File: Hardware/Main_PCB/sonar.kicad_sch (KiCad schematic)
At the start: 11 parts, among them U2 TUSS4470TRTJT

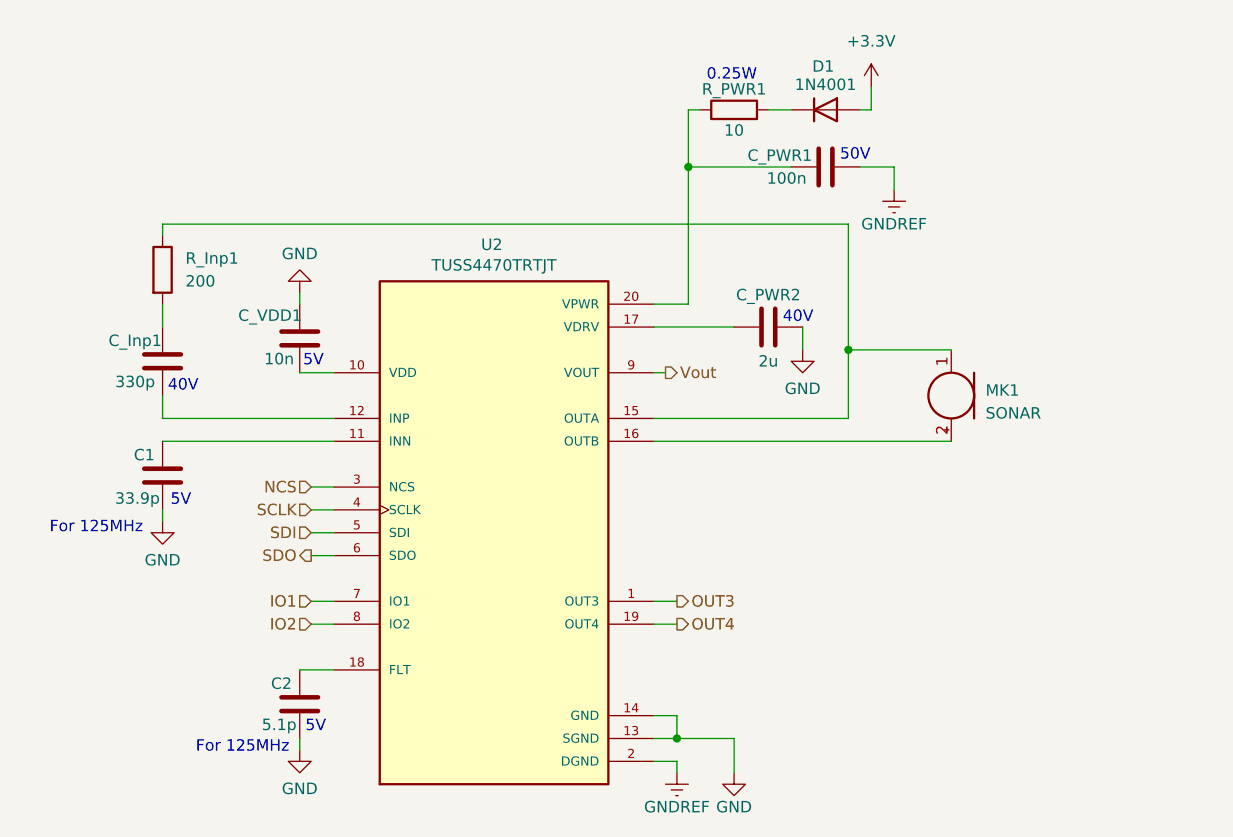
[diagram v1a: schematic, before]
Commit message: Trustworthy version of the MAIN PCB schematic
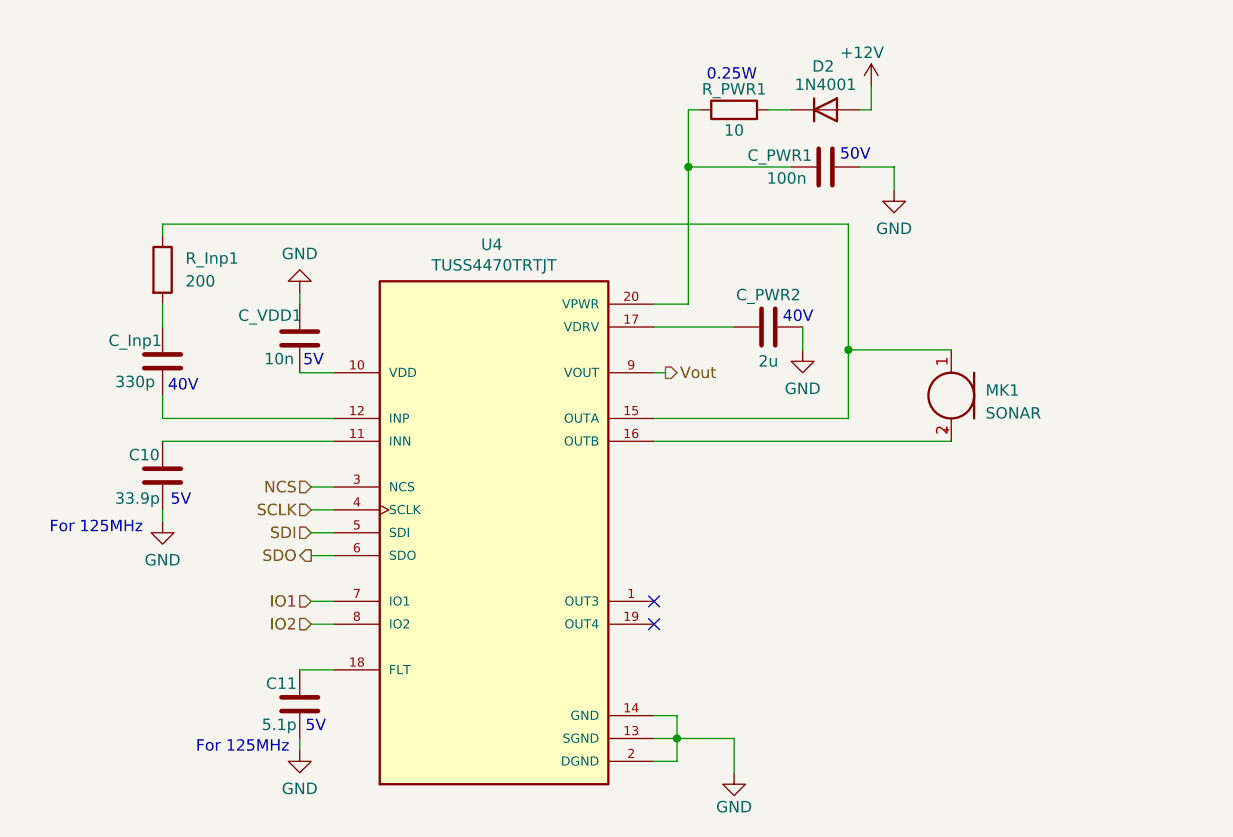
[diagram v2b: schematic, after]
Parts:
- renumbered C1 to C10, C2 to C11, D1 to D2, U2 to U4
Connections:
- net GNDREF is gone; now on net GND: C_PWR1.2, U4.2 (DGND)
- net +3.3V renamed +12V
- net OUT3: no longer names the net of U4.1 (OUT3)
- net OUT4: no longer names the net of U4.19 (OUT4)
- no-connect marks 0 -> 2

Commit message: Added some footprints
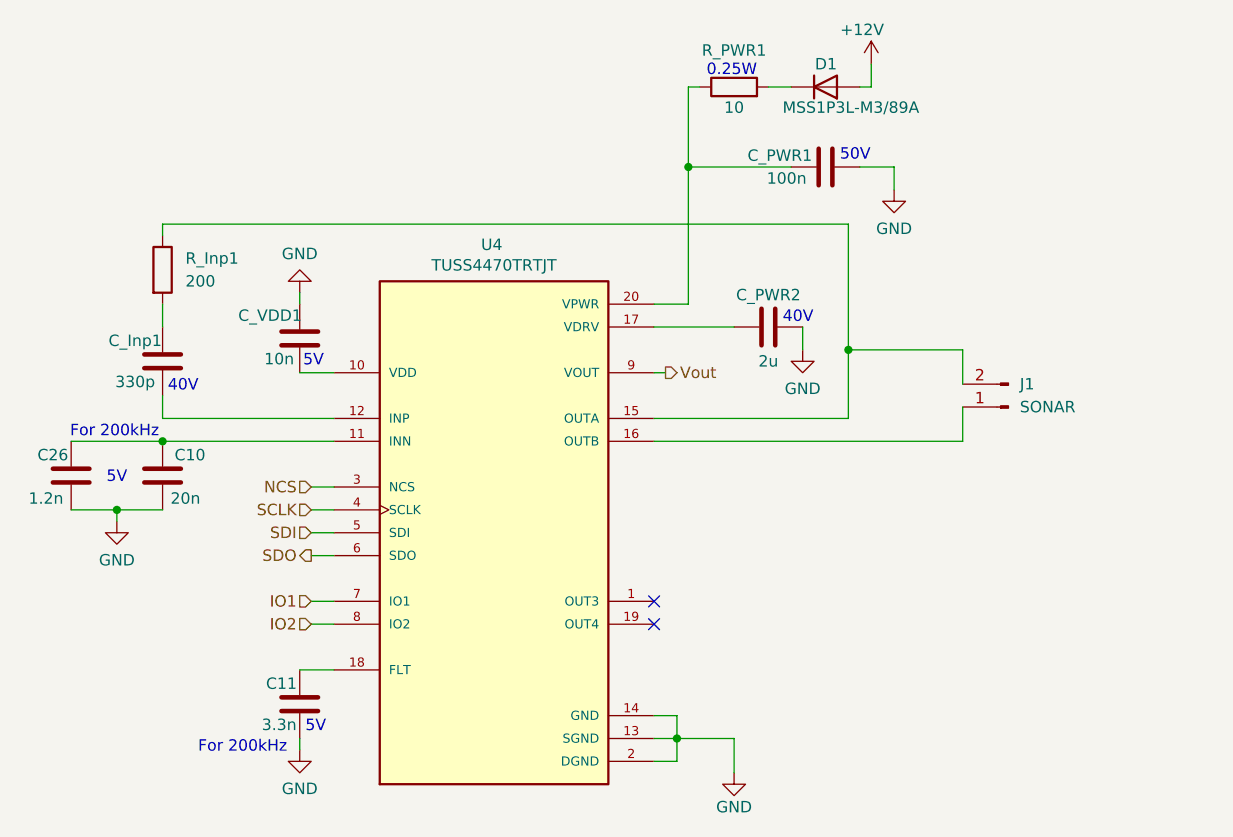
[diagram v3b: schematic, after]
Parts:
- removed D2: 1N4001, symbol Device:D
- removed MK1: SONAR, symbol Device:Microphone
- added C26: 1.2n, Capacitor_SMD:C_0603_1608Metric_Pad1.08x0.95mm_HandSolder, symbol Device:C
- added D1: MSS1P3L-M3/89A, Diode_SMD:Vishay_SMPA, symbol Diode:S2JTR
- added J1: SONAR, Connector_JST:JST_PH_B2B-PH-K_1x02_P2.00mm_Vertical, symbol Connector:Conn_01x02_Pin
- C10: value 33.9p -> 20n; footprint (none) -> Capacitor_SMD:C_0805_2012Metric_Pad1.18x1.45mm_HandSolder
- C11: value 5.1p -> 3.3n; footprint (none) -> Capacitor_SMD:C_0805_2012Metric_Pad1.18x1.45mm_HandSolder
- C_Inp1, C_PWR1, C_VDD1, R_PWR1: footprint (none) -> Capacitor_SMD:C_0805_2012Metric_Pad1.18x1.45mm_HandSolder
- C_PWR2: footprint (none) -> Capacitor_SMD:C_0603_1608Metric_Pad1.08x0.95mm_HandSolder
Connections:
- net +12V: now also D1.2 (A)
- net GND: now also C26.1
- net at C10.2, U4.11 (INN): now also C26.2
- net at R_Inp1.1, U4.15 (OUTA): now also J1.2 (Pin_2)
- net at U4.16 (OUTB): now also J1.1 (Pin_1)
- net at R_PWR1.2: now also D1.1 (K)
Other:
- note added: "For 200kHz"
- note removed: "For 125MHz"
- moved on the sheet: R_PWR1

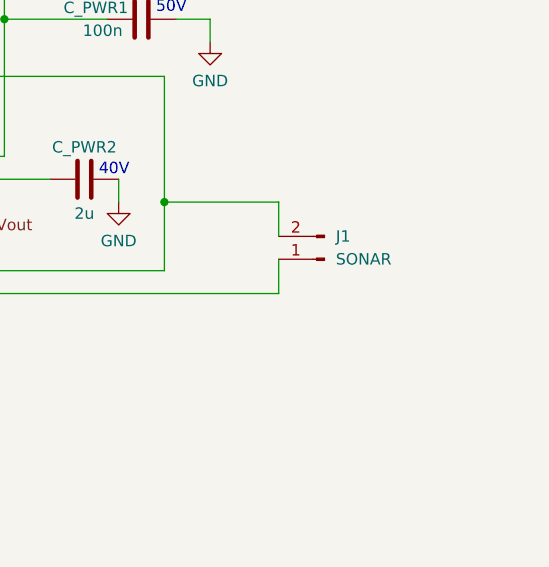
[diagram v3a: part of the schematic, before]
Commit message: Updated sonar.kicad_sch with a new sonar connector
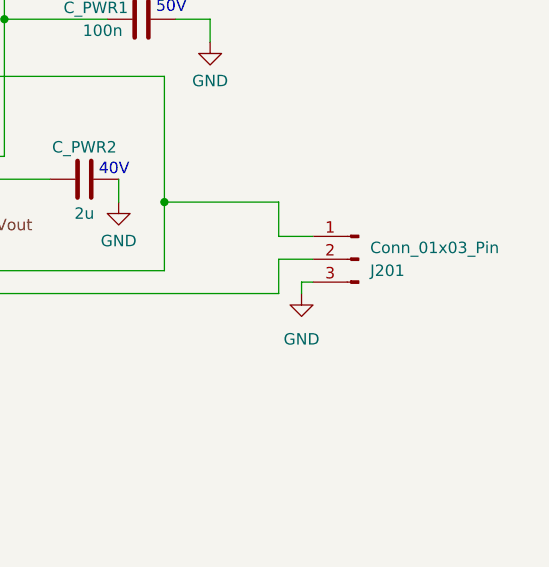
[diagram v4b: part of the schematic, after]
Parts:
- removed J1: SONAR, Connector_JST:JST_PH_B2B-PH-K_1x02_P2.00mm_Vertical, symbol Connector:Conn_01x02_Pin
- added J201: Conn_01x03_Pin, Connector_JST:JST_PH_B3B-PH-K_1x03_P2.00mm_Vertical, symbol Connector:Conn_01x03_Pin
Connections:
- net GND: now also J201.3 (Pin_3)
- net at R_Inp1.1, U4.15 (OUTA): now also J201.1 (Pin_1)
- net at U4.16 (OUTB): now also J201.2 (Pin_2)
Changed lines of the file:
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@@
+	(wire
+		(pts
+			(xy 143.51 57.15) (xy 147.32 57.15)
+		)
+		(stroke
+			(width 0)
+			(type default)
+		)
+	)
 	(wire
 		(pts
@@
 	(wire
 		(pts
+			(xy 146.05 59.69) (xy 146.05 60.96)
+		)
+		(stroke
+			(width 0)
+			(type default)
+		)
+	)
+	(wire
+		(pts
 			(xy 143.51 50.8) (xy 143.51 54.61)
 		)
@@
 	(wire
 		(pts
+			(xy 146.05 59.69) (xy 147.32 59.69)
+		)
+		(stroke
+			(width 0)
+			(type default)
+		)
+	)
+	(wire
+		(pts
 			(xy 113.03 30.48) (xy 124.46 30.48)
 		)
@@
 		(pts
 			(xy 109.22 53.34) (xy 110.49 53.34)
+		)
+		(stroke
+			(width 0)
+			(type default)
+		)
+	)
+	(wire
+		(pts
+			(xy 143.51 54.61) (xy 147.32 54.61)
 		)
 		(stroke
@@
 	)
 	(symbol
+		(lib_id "Connector:Conn_01x03_Pin")
+		(at 152.4 57.15 0)
+		(mirror y)
+		(unit 1)
+		(exclude_from_sim no)
+		(in_bom yes)
+		(on_board yes)
+		(dnp no)
+		(property "Reference" "J201"
+			(at 153.67 58.4201 0)
+			(effects
+				(font
+					(size 1.27 1.27)
+				)
+				(justify right)
+			)
+		)
+		(property "Value" "Conn_01x03_Pin"
+			(at 153.67 55.8801 0)
+			(effects
+				(font
+					(size 1.27 1.27)
+				)
+				(justify right)
+			)
+		)
+		(property "Footprint" "Connector_JST:JST_PH_B3B-PH-K_1x03_P2.00mm_Vertical"
+			(at 152.4 57.15 0)
+			(effects
+				(font
+					(size 1.27 1.27)
+				)
+				(hide yes)
+			)
+		)
+		(property "Datasheet" "~"
+			(at 152.4 57.15 0)
+			(effects
+				(font
+					(size 1.27 1.27)
+				)
+				(hide yes)
+			)
+		)
+		(property "Description" "Generic connector, single row, 01x03, script generated"
+			(at 152.4 57.15 0)
+			(effects
+				(font
+					(size 1.27 1.27)
+				)
+				(hide yes)
+			)
+		)
+		(pin "3"
+		)
+		(pin "2"
+		)
+		(pin "1"
+		)
+		(instances
+			(project "Main_PCB"
+				(path "/90d7beec-e1a2-46f8-bbb2-6b8f3489db10/fb18f23d-afe6-46fa-a762-d7c19ead7543"
+					(reference "J201")
+					(unit 1)
+				)
+			)
+		)
+	)
+	(symbol
 		(lib_id "Device:R")
 		(at 54.61 41.91 0)
@@
 	)
 	(symbol
+		(lib_id "power:GND")
+		(at 146.05 60.96 0)
+		(unit 1)
+		(exclude_from_sim no)
+		(in_bom yes)
+		(on_board yes)
+		(dnp no)
+		(fields_autoplaced yes)
+		(property "Reference" "#PWR0201"
+			(at 146.05 67.31 0)
+			(effects
+				(font
+					(size 1.27 1.27)
+				)
+				(hide yes)
+			)
+		)
+		(property "Value" "GND"
+			(at 146.05 66.04 0)
+			(effects
+				(font
+					(size 1.27 1.27)
+				)
+			)
+		)
+		(property "Footprint" ""
+			(at 146.05 60.96 0)
+			(effects
+				(font
+					(size 1.27 1.27)
+				)
+				(hide yes)
+			)
+		)
+		(property "Datasheet" ""
+			(at 146.05 60.96 0)
+			(effects
+				(font
+					(size 1.27 1.27)
+				)
+				(hide yes)
+			)
+		)
+		(property "Description" "Power symbol creates a global label with name \"GND\" , ground"
+			(at 146.05 60.96 0)
+			(effects
+				(font
+					(size 1.27 1.27)
+				)
+				(hide yes)
+			)
+		)
+		(pin "1"
+		)
+		(instances
+			(project ""
+				(path "/90d7beec-e1a2-46f8-bbb2-6b8f3489db10/fb18f23d-afe6-46fa-a762-d7c19ead7543"
+					(reference "#PWR0201")
+					(unit 1)
+				)
+			)
+		)
+	)
+	(symbol
 		(lib_id "Device:C")
 		(at 54.61 52.07 180)
@@
 					(unit 1)
 				)
-			)
-		)
-	)
-	(symbol
-		(lib_id "Connector:Conn_01x02_Pin")
-		(at 148.59 57.15 180)
-		(unit 1)
-		(exclude_from_sim no)
-		(in_bom yes)
-		(on_board yes)
-		(dnp no)
-		(fields_autoplaced yes)
-		(property "Reference" "J1"
-			(at 149.86 54.6099 0)
-			(effects
-				(font
-					(size 1.27 1.27)
-				)
-				(justify right)
-			)
-		)
-		(property "Value" "SONAR"
-			(at 149.86 57.1499 0)
-			(effects
-				(font
-					(size 1.27 1.27)
-				)
-				(justify right)
-			)
-		)
-		(property "Footprint" "Connector_JST:JST_PH_B2B-PH-K_1x02_P2.00mm_Vertical"
-			(at 148.59 57.15 0)
-			(effects
-				(font
-					(size 1.27 1.27)
-				)
-				(hide yes)
-			)
-		)
-		(property "Datasheet" "~"
-			(at 148.59 57.15 0)
-			(effects
-				(font
-					(size 1.27 1.27)
-				)
-				(hide yes)
-			)
-		)
-		(property "Description" "Generic connector, single row, 01x02, script generated"
-			(at 148.59 57.15 0)
-			(effects
-				(font
-					(size 1.27 1.27)
-				)
-				(hide yes)
-			)
-		)
-		(pin "1"
-		)
-		(pin "2"
-		)
-		(instances
-			(project ""
-				(path "/90d7beec-e1a2-46f8-bbb2-6b8f3489db10/fb18f23d-afe6-46fa-a762-d7c19ead7543"
-					(reference "J1")
-					(unit 1)
-				)
